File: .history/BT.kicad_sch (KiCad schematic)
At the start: 85 parts, among them J1 Conn_01x05_Pin, J2 Conn_01x03_Pin, J3 Conn_01x06_Pin, J5 Conn_02x03_Odd_Even, K1 AGQ200S12Z, Q1 BSS123, U1 PCM5100A, U2 ESP32-WROOM-32U, U3 TLV4888DR, U4 AP64060WU-7, U6 TPS7A4701, U7 AP64060WU-7, Y1 XO32

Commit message: clean up
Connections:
- net +12V_FUSED: now reaches C18.1, F1.1, U4.4 (EN), U4.5 (VIN)
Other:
- moved on the sheet: C17, C30, L1, L2, R18, R20, R31, R5

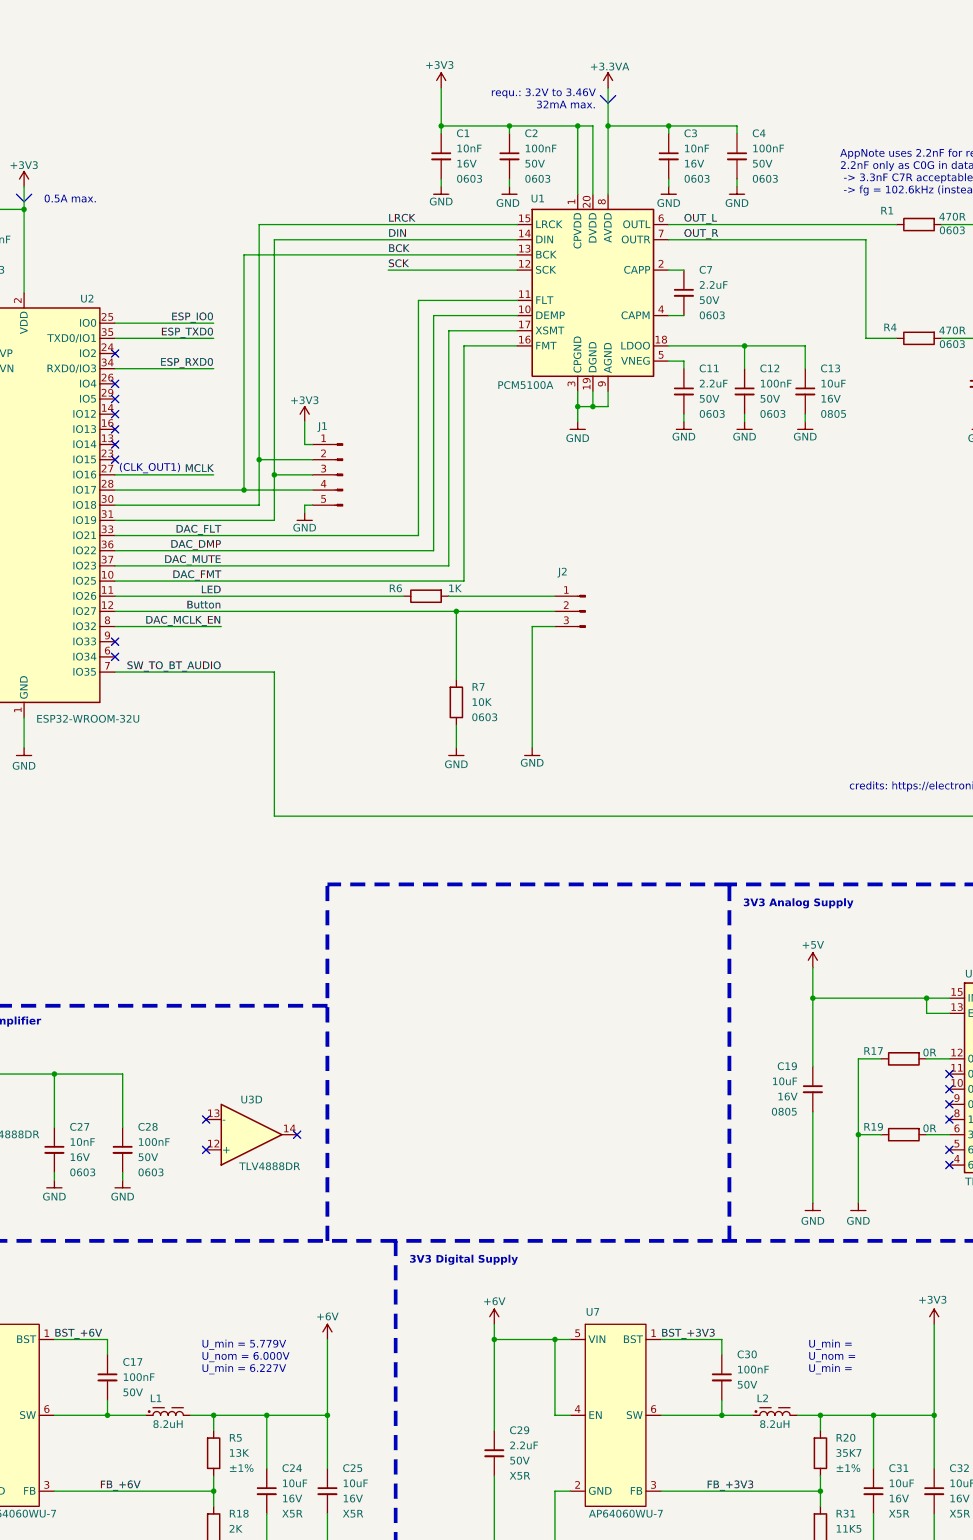
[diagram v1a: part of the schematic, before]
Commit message: integrated DAC in database
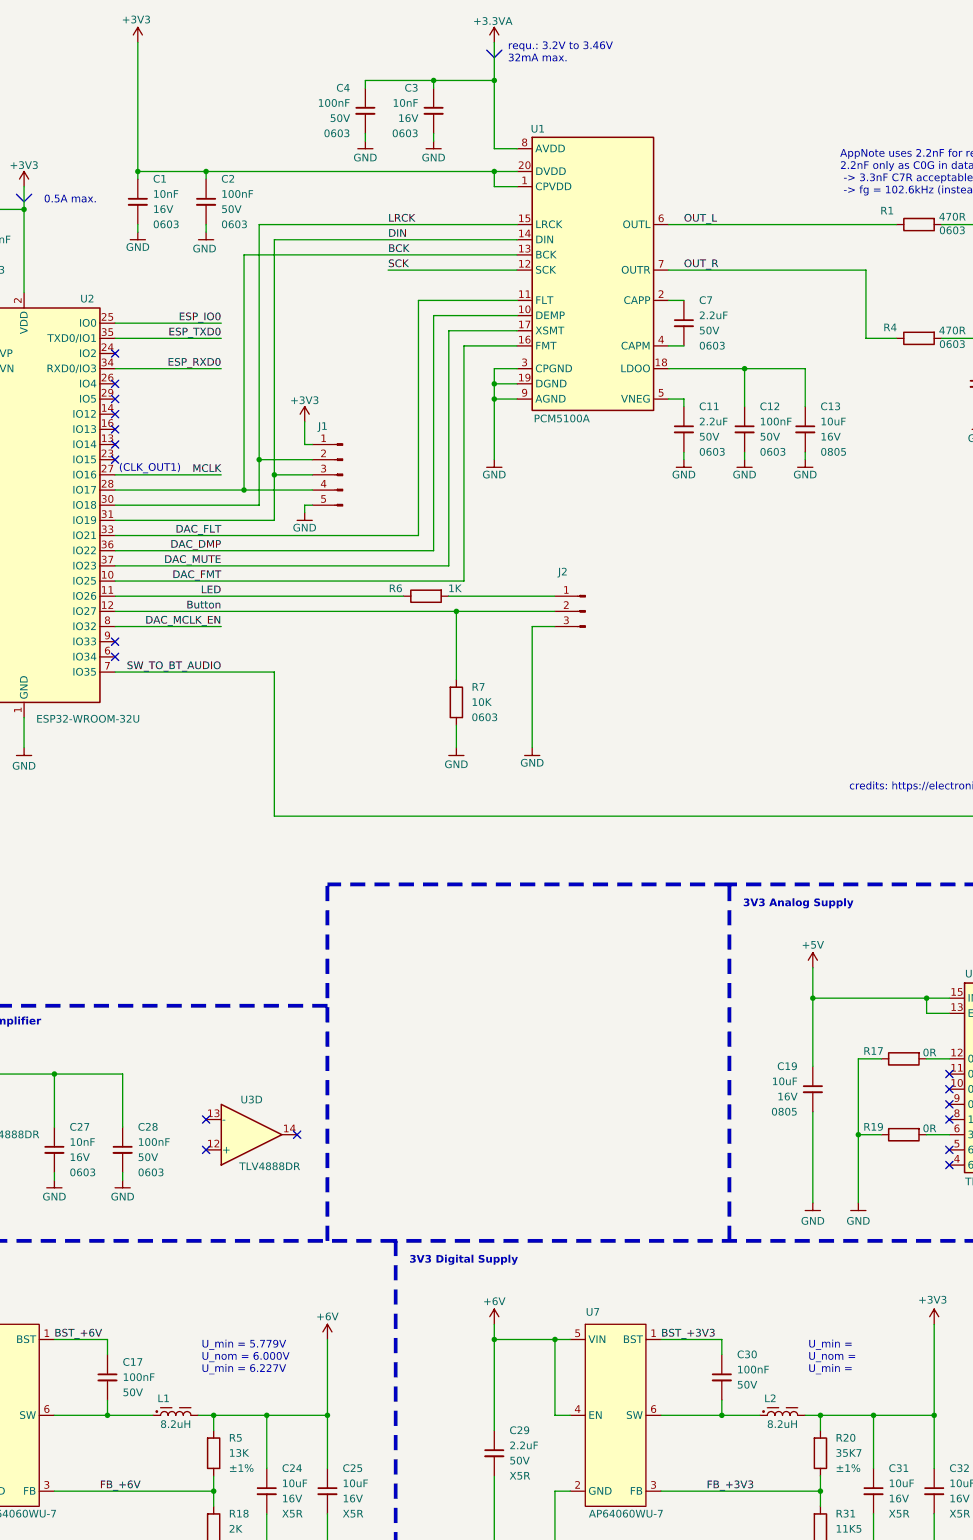
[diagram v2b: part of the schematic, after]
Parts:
- U1: footprint Package_SO:TSSOP-20_4.4x6.5mm_P0.65mm -> NRD_IC_DATA:PCM510xx; symbol Audio:PCM5100A -> NRD_IC_DATA:PCM5100A
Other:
- moved on the sheet: C1, C2, C3, C4, L1, L2, U1

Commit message: wip
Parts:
- removed C14, C15: 220nF, NRD_CAP:C_0603, symbol NRD_C_0603:CL10B224JO8NNNC
- removed C17, C28, C30: 100nF, NRD_CAP:C_0603, symbol NRD_C_0603:CL10B104KB8NNNC
- removed C18, C29: 2.2uF, NRD_CAP:C_0603, symbol NRD_C_0603:CL10A225KB8NNNC
- removed C19, C24, C25, C31, C32: 10uF, NRD_CAP:C_0805, symbol NRD_C_0805:CL21A106KOFNNNE
- removed C20, C21: 22uF, NRD_CAP:C_0805, symbol NRD_C_0805:CL21A226MAYNNNE
- removed C26: 1uF, NRD_CAP:C_0603, symbol NRD_C_0603:CL10B105KA8NNNC
- removed J5: Conn_02x03_Odd_Even, Connector_PinHeader_1.27mm:PinHeader_2x03_P1.27mm_Vertical_SMD, symbol Connector_Generic:Conn_02x03_Odd_Even
- removed L1, L2: 8.2uH, NRD_IND:74438367082, symbol NRD_IND:74438367082
- removed Q1: BSS123, Package_TO_SOT_SMD:SOT-23, symbol Transistor_FET:BSS123
- removed R17, R19: 0R, NRD_RES:R_0603, symbol NRD_R_0603:RC0603FR-070RL
- removed R18: 2K, NRD_RES:R_0603, symbol NRD_R_0603:RC0603FR-072KL
- removed R2: 10K, NRD_R_Var:3296P, symbol NRD_R_Var:3296P-1-103LF
- removed R20: 35K7, NRD_RES:R_0603, symbol NRD_R_0603:RC0603FR-0735K7L
- removed R31: 11K5, NRD_RES:R_0603, symbol NRD_R_0603:RC0603FR-0711K5L
- removed R5: 13K, NRD_RES:R_0603, symbol NRD_R_0603:RC0603FR-0713KL
- removed U2: ESP32-WROOM-32U, RF_Module:ESP32-WROOM-32U, symbol RF_Module:ESP32-WROOM-32U
- removed U4, U7: AP64060WU-7, NRD_IC_DCDC:AP6406x, symbol NRD_IC_DCDC:AP64060WU-7
- removed U6: TPS7A4701, NRD_LDO:TPS7A47x, symbol NRD_LDO:TPS7A4701
- added C14, C15, C22, C33, C34, C36: 2.2uF, NRD_CAP:C_0805, symbol NRD_C_0805:CL21B225KAFNNNE
- added C17, C19, C21, C23, C26: 4.7uF, NRD_CAP:C_1206, symbol NRD_C_1206:CL31B475KBHNNNE
- added C18, C20, C31, C32, C35: 100nF, NRD_CAP:C_0603, symbol NRD_C_0603:CL10B104KB8NNNC
- added C24, C25, C29, C30: 22uF, NRD_CAP:C_1206, symbol NRD_C_1206:CL31B226KPHNNNE
- added FB1, FB3: 4k7@100MHz, symbol Device:FerriteBead
- added FB2, FB4: 4k7@100MHz, Inductor_SMD:L_0805_2012Metric, symbol Device:FerriteBead
- added J4: Boxed_Header_02x03_SMT, NRD_CON:Boxed_Header_02x03_SMT, symbol NRD_CON:Boxed_Header_02x03_SMT
- added Q1: BSS123, NRD_MOSFET:BSS123, symbol NRD_MOSFET:BSS123
- added R17, R18, R19: 10K, NRD_RES:R_0603, symbol NRD_R_0603:RC0603FR-0710KL
- added R2: 34K, NRD_RES:R_0603, symbol NRD_R_0603:RC0603FR-0734KL
- added R20: 2K, NRD_RES:R_0603, symbol NRD_R_0603:RC0603FR-072KL
- added R31: 21K, NRD_RES:R_0603, symbol NRD_R_0603:RC0603FR-0721KL
- added R32: 13K7, NRD_RES:R_0603, symbol NRD_R_0603:RC0603FR-0713K7L
- added R5: 14K3, NRD_RES:R_0603, symbol NRD_R_0603:RC0603FR-0714K3L
- added RV1: 10K, Potentiometer_SMD:Potentiometer_Bourns_TC33X_Vertical, symbol Device:R_Potentiometer_Trim
- added U2: ESP32-WROOM-32U, NRD_IC_MCU:WROOM_32U, symbol NRD_IC_MCU:ESP32-WROOM-32UE-N8
- added U4, U5: TLVM23615RDNR, NRD_IC_DCDC:TxxM336x5, symbol NRD_IC_DCDC:TLVM23615RDNR
- added U6: RAA214220, NRD_LDO:RAA214220, symbol NRD_LDO:RAA214220
- C11, C7: footprint NRD_CAP:C_0603 -> NRD_CAP:C_0805; symbol NRD_C_0603:CL10A225KB8NNNC -> NRD_C_0805:CL21B225KAFNNNE; Dielectric X5R -> X7R; Manufacturer Part Number CL10A225KB8NNNC -> CL21B225KAFNNNE; Maximum Operating Temperature [°C] 85 -> 125; Package 0603 -> 0805; Voltage 50V -> 25V; Voltage [V] 50 -> 25
- C13: symbol NRD_C_0805:CL21A106KOFNNNE -> NRD_C_0805:CL21B106KOQNNNG; Dielectric X5R -> X7R; Manufacturer Part Number CL21A106KOFNNNE -> CL21B106KOQNNNG; Maximum Operating Temperature [°C] 85 -> 125
- J3: value Conn_01x06_Pin -> S6B-PH-K-S; footprint Connector_JST:JST_PH_S6B-PH-K_1x06_P2.00mm_Horizontal -> NRD_CON:S6B-PH-K-S; symbol Connector:Conn_01x06_Pin -> NRD_CON:S6B-PH-K-S; Manufacturer (none) -> JST; Manufacturer Part Number (none) -> S6B-PH-K-S; Maximum Operating Temperature [°C] (none) -> 85; Minimum Operating Temperature [°C] (none) -> -25; RoHS (none) -> Yes
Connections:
- net +12V_FUSED is gone; now on net +12V: F1.1
- net +12V: now also C17.1, C18.1, C19.1, C20.1, U4.2 (EN), U4.3 (VIN), U5.2 (EN), U5.3 (VIN); no longer F1.2, J3.1 (Pin_1)
- net +3V3: now also C24.1, C25.1, C31.1, J4.2 (Pin_2), R2.1, U2.2 (VDD), U4.4 (VOUT), U6.1 (VIN), U6.3 (EN)
- net +6V: now also C29.1, C30.1, C34.1, FB3.2, R17.1, U5.4 (VOUT)
- net BCK: now also U2.28 (IO17)
- net Button: now also U2.12 (IO27)
- net DAC_DMP: now also U2.36 (IO22)
- net DAC_FLT: now also U2.33 (IO21)
- net DAC_FMT: now also U2.10 (IO25)
- net DAC_MCLK_EN: now also U2.8 (IO32)
- net DAC_MUTE: now also U2.37 (IO23)
- net DIN: now also U2.31 (IO19)
- net ESP_EN: now also J4.1 (Pin_1), U2.3 (EN)
- net ESP_IO0: now also J4.6 (Pin_6), U2.25 (IO0)
- net ESP_RXD0: now also J4.5 (Pin_5), U2.34 (RXD0/IO3)
- net ESP_TXD0: now also J4.3 (Pin_3), U2.35 (TXD0/IO1)
- net GND: now also C17.2, C18.2, C19.2, C20.2, C21.2, C22.2, C23.2, C24.2, C25.2, C26.2, C29.2, C30.2, C31.2, C32.2, C33.2, C34.2, C35.2, C36.2, J4.4 (Pin_4), Q1.2 (S), R18.2, R19.2, R20.2, R32.2, R5.2, RV1.2, U2.1 (GND), U2.15 (GND), U2.38 (GND), U2.39 (EP), U4.10 (GND), U5.10 (GND), U6.2 (GND)
- net LED: now also U2.11 (IO26)
- net LRCK: now also U2.30 (IO18)
- net MCLK: now also U2.27 (IO16)
- net OUT_L_CON: now also C14.1
- net OUT_R_CON: now also C15.1
- net SW_TO_BT_AUDIO: now also Q1.1 (G), U2.7 (IO35)
- net at R30.1, TP3.1, U3.8: now also C15.2
- net at D1.2 (A), K1.8: now also Q1.3 (D)
- net at R12.1, R21.2, TP2.1: now also C14.2, RV1.1
- net at R25.1, R26.2, R29.2: now also RV1.3
- net +5V: no longer names the net of C27.1, U3.4 (V+)
- net +5V: now also C36.1, FB4.1
- new net: R2.2, R5.1, U4.9 (FB)
- new net: C35.1, FB3.1, FB4.2
- new net: C26.1, U5.8 (VCC)
- new net: R18.1, U4.11 (RT)
- new net: C23.1, U4.8 (VCC)
- new net: R17.2, R20.1, U5.9 (FB)
- new net: C32.1, FB1.1, FB2.2
- new net: C21.1, C22.1, FB1.2, R31.1, U6.5 (VOUT)
- new net: R31.2, R32.1, U6.4 (ADJ)
- new net: R19.1, U5.11 (RT)
- new net +3V3A: C33.1, FB2.1
- new net KL30: F1.2, J3.1 (Pin_1)
- no-connect marks 26 -> 28
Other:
- note added: "+3V3 Supply"
- note added: "0.520mA"
- note added: "1.5A"
- note added: "12V"
- note added: "3.0V to 3.6V"
- note added: "3.10V to 3.46V 20mA max."
- note added: "3.1V"
- note added: "3.46V"
- note added: "32mA"
- note added: "32mA max."
- note added: "6.0V"
- note added: "Analog Suppl DAC"
- note added: "DAC Clock"
- note added: "DAC_analog_supply"
- note added: "DC"
- note added: "LDO"
- note added: "MCU / DAC_dig_supply"
- note added: "OPAmps"
- note added: "Power Tree"
- note added: "RAA2142204GP3#JA0"
- note added: "TLVM23615RDNR"
- note added: "Uo_max = 3.460V Uo_nom = 3.378V Uo_min = 3.297V"
- note added: "Uo_max = 6.16V Uo_nom = 6.00V Uo_min = 5.84V"
- note added: "Uo_min = 3.008V Uo_nom = 3.107V Uo_max = 3.208V"
- note added: "Worst case Dropout Voltage (min.): U_+3V3: min (-> 3.297V) U_+3V3A: max ( -> 3.208V) => U_dropout = 89mV"
- note added: "requ.: 3.0V to 3.46V 32mA max."
- note removed: "3V3 Analog Supply"
- note removed: "3V3 Digital Supply"
- note removed: "6.0V Voltage Regulator"
- note removed: "DAC CLK"
- note removed: "U_min = 5.779V U_nom = 6.000V U_min = 6.227V"
- note removed: "U_min = U_nom = U_min ="
- note removed: "requ.: 3.2V to 3.46V 32mA max."
- moved on the sheet: C4, C5, C6, F1, H1, H2, H3, J3, TP1, U3D, U3E
